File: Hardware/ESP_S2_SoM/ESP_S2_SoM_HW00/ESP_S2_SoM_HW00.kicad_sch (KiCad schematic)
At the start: 0 parts

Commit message: lots of work on routing
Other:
- sheet 100_Connectors ports: added BATTERY_TEMP; removed none
- sheet 200_1S_Charger ports: added BATTERY_TEMP; removed none
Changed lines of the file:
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@@
+    (stroke (width 0) (type default))
+  )
+  (wire (pts (xy 101.6 58.42) (xy 127 58.42))
     (stroke (width 0) (type default))
   )
@@
       (effects (font (size 1.27 1.27)) (justify left))
     )
+    (pin "BATTERY_TEMP" input (at 127 58.42 180)
+      (effects (font (size 1.27 1.27)) (justify left))
+    )
     (instances
       (project "ESP_S2_SoM_HW00"
@@
       (effects (font (size 1.27 1.27)) (justify right))
     )
+    (pin "BATTERY_TEMP" output (at 101.6 58.42 0)
+      (effects (font (size 1.27 1.27)) (justify right))
+    )

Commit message: Working on PSoM ESP32S2
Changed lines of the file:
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@@
     (stroke (width 0) (type default))
+  )
+  (label "3V3" (at 88.9 22.86 90) (fields_autoplaced)
+    (effects (font (size 1.27 1.27)) (justify left bottom))
+  )
+  (label "3V3" (at 88.9 99.06 90) (fields_autoplaced)
+    (effects (font (size 1.27 1.27)) (justify left bottom))
+  )
+  (label "3V3" (at 160.02 99.06 90) (fields_autoplaced)
+    (effects (font (size 1.27 1.27)) (justify left bottom))
+  )
+  (label "VBUS" (at 96.52 22.86 90) (fields_autoplaced)
+    (effects (font (size 1.27 1.27)) (justify left bottom))
+  )
+  (label "VSYS" (at 147.32 22.86 90) (fields_autoplaced)
+    (effects (font (size 1.27 1.27)) (justify left bottom))
+  )
+  (label "VBUS" (at 152.4 22.86 90) (fields_autoplaced)
+    (effects (font (size 1.27 1.27)) (justify left bottom))
+  )
+  (label "VSYS" (at 91.44 22.86 90) (fields_autoplaced)
+    (effects (font (size 1.27 1.27)) (justify left bottom))
+  )
+  (label "VSYS" (at 91.44 99.06 90) (fields_autoplaced)
+    (effects (font (size 1.27 1.27)) (justify left bottom))
+  )
+  (label "VBAT" (at 149.86 22.86 90) (fields_autoplaced)
+    (effects (font (size 1.27 1.27)) (justify left bottom))
+  )
+  (label "VBAT" (at 93.98 22.86 90) (fields_autoplaced)
+    (effects (font (size 1.27 1.27)) (justify left bottom))
   )
   (symbol (lib_id "power:GND") (at 167.64 154.94 0) (unit 1)

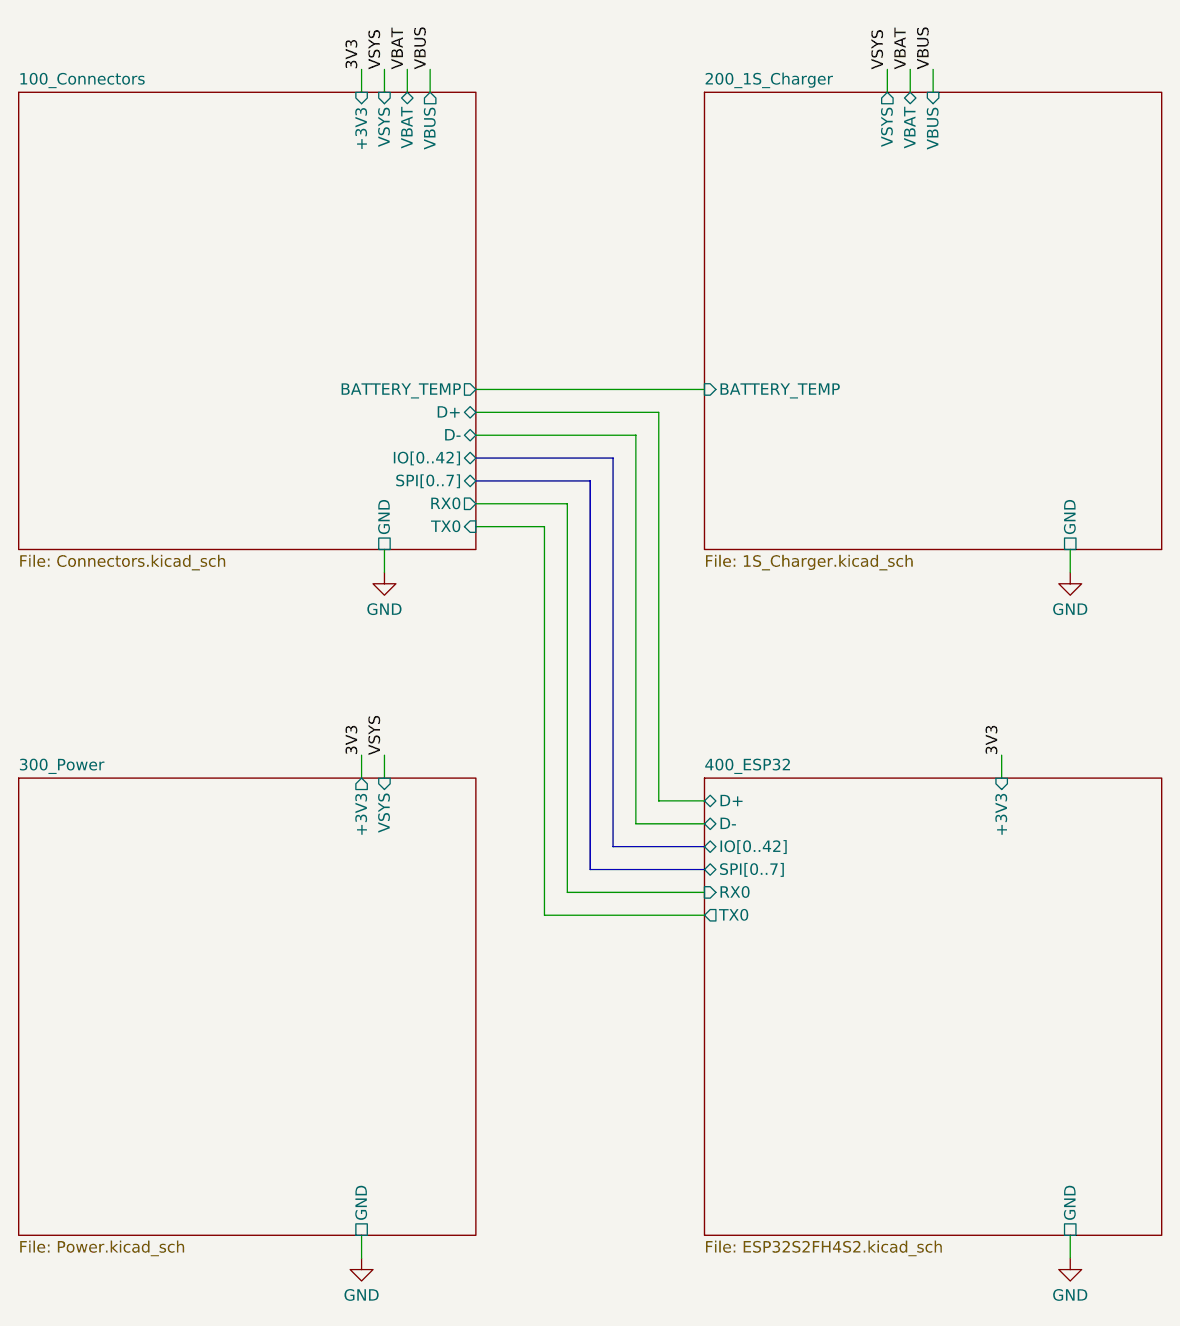
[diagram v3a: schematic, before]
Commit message: quick pinout adjustement
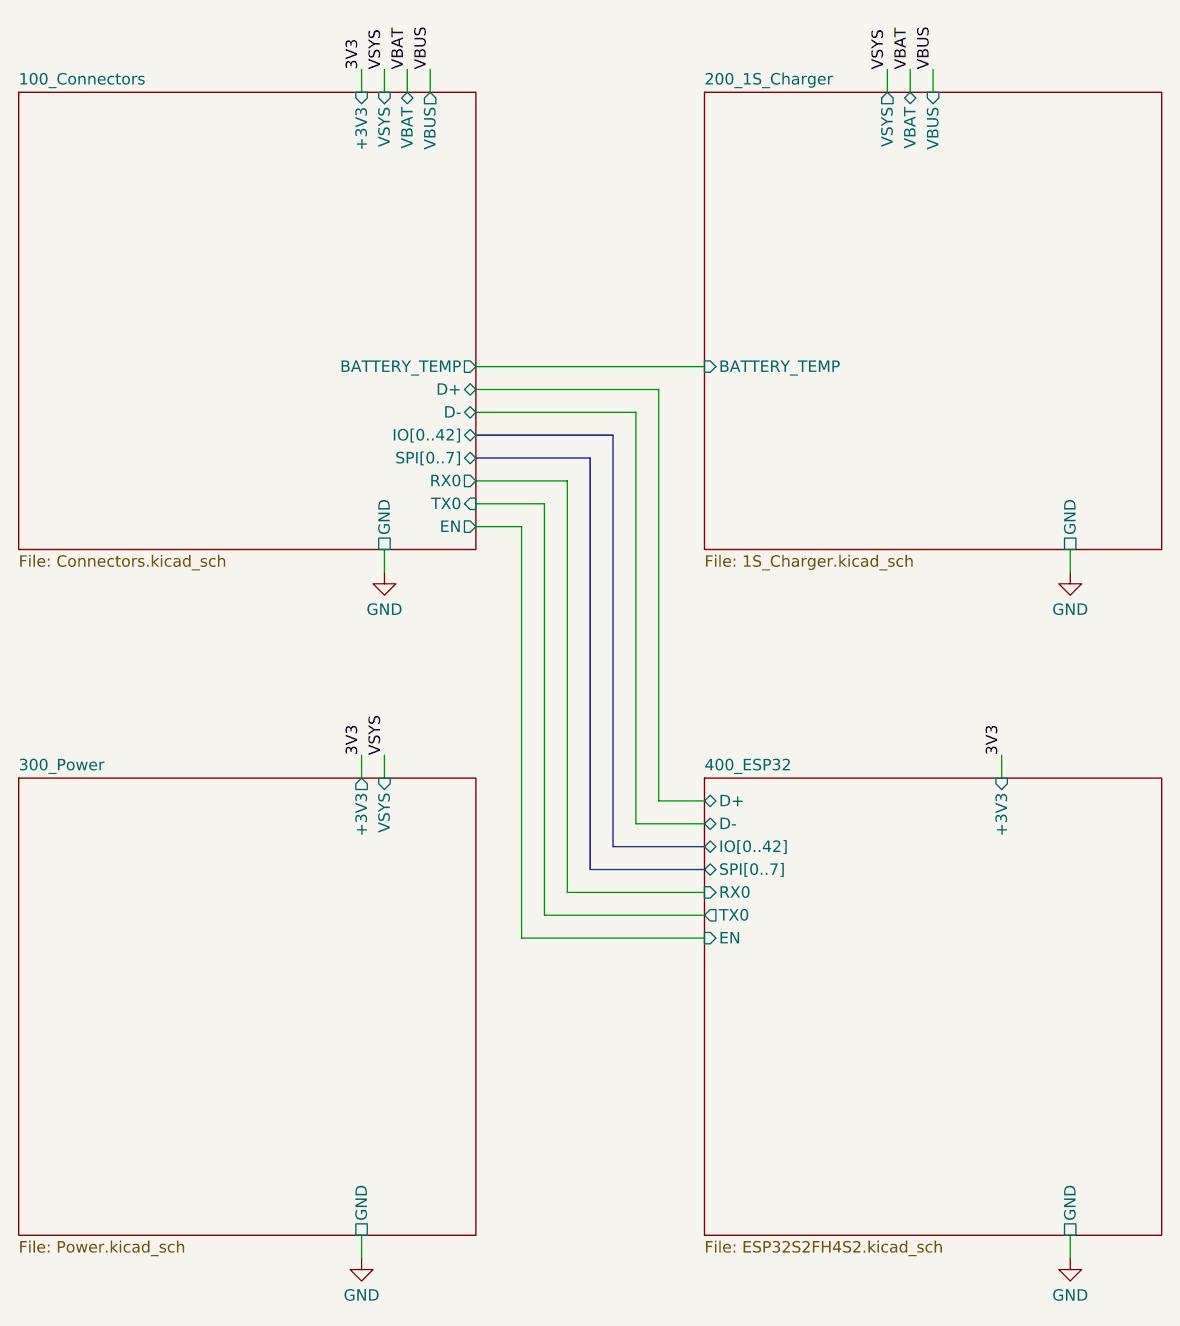
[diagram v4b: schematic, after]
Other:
- sheet 100_Connectors ports: added EN; removed none
- sheet 400_ESP32 ports: added EN; removed none
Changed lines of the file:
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@@
     (company "PumaCorp")
   )
+  (wire (pts (xy 127 114.3) (xy 111.76 114.3))
+    (stroke (width 0) (type default))
+  )
+  (wire (pts (xy 147.32 22.86) (xy 147.32 25.4))
+    (stroke (width 0) (type default))
+  )
+  (bus (pts (xy 114.3 111.76) (xy 127 111.76))
+    (stroke (width 0) (type default))
+  )
+  (wire (pts (xy 167.64 152.4) (xy 167.64 154.94))
+    (stroke (width 0) (type default))
+  )
+  (wire (pts (xy 93.98 22.86) (xy 93.98 25.4))
+    (stroke (width 0) (type default))
+  )
+  (wire (pts (xy 109.22 71.12) (xy 109.22 116.84))
+    (stroke (width 0) (type default))
+  )
+  (wire (pts (xy 96.52 22.86) (xy 96.52 25.4))
+    (stroke (width 0) (type default))
+  )
+  (wire (pts (xy 101.6 73.66) (xy 106.68 73.66))
+    (stroke (width 0) (type default))
+  )
+  (wire (pts (xy 91.44 76.2) (xy 91.44 78.74))
+    (stroke (width 0) (type default))
+  )
+  (wire (pts (xy 121.92 58.42) (xy 101.6 58.42))
+    (stroke (width 0) (type default))
+  )
+  (wire (pts (xy 106.68 73.66) (xy 106.68 119.38))
+    (stroke (width 0) (type default))
+  )
+  (wire (pts (xy 121.92 58.42) (xy 121.92 104.14))
+    (stroke (width 0) (type default))
+  )
+  (wire (pts (xy 111.76 114.3) (xy 111.76 68.58))
+    (stroke (width 0) (type default))
+  )
+  (wire (pts (xy 88.9 152.4) (xy 88.9 154.94))
+    (stroke (width 0) (type default))
+  )
+  (bus (pts (xy 116.84 109.22) (xy 116.84 63.5))
+    (stroke (width 0) (type default))
+  )
+  (bus (pts (xy 127 109.22) (xy 116.84 109.22))
+    (stroke (width 0) (type default))
+  )
+  (wire (pts (xy 106.68 119.38) (xy 127 119.38))
+    (stroke (width 0) (type default))
+  )
+  (wire (pts (xy 111.76 68.58) (xy 101.6 68.58))
+    (stroke (width 0) (type default))
+  )
   (wire (pts (xy 119.38 106.68) (xy 127 106.68))
     (stroke (width 0) (type default))
   )
-  (wire (pts (xy 147.32 22.86) (xy 147.32 25.4))
-    (stroke (width 0) (type default))
-  )
-  (wire (pts (xy 167.64 152.4) (xy 167.64 154.94))
-    (stroke (width 0) (type default))
-  )
-  (wire (pts (xy 93.98 22.86) (xy 93.98 25.4))
-    (stroke (width 0) (type default))
-  )
-  (wire (pts (xy 101.6 73.66) (xy 109.22 73.66))
-    (stroke (width 0) (type default))
-  )
-  (wire (pts (xy 96.52 22.86) (xy 96.52 25.4))
-    (stroke (width 0) (type default))
-  )
-  (wire (pts (xy 111.76 71.12) (xy 101.6 71.12))
-    (stroke (width 0) (type default))
-  )
-  (wire (pts (xy 119.38 63.5) (xy 119.38 106.68))
-    (stroke (width 0) (type default))
-  )
-  (wire (pts (xy 91.44 76.2) (xy 91.44 78.74))
-    (stroke (width 0) (type default))
-  )
-  (wire (pts (xy 121.92 104.14) (xy 121.92 60.96))
-    (stroke (width 0) (type default))
-  )
-  (bus (pts (xy 114.3 68.58) (xy 114.3 111.76))
-    (stroke (width 0) (type default))
-  )
-  (wire (pts (xy 121.92 60.96) (xy 101.6 60.96))
-    (stroke (width 0) (type default))
-  )
-  (wire (pts (xy 88.9 152.4) (xy 88.9 154.94))
+  (bus (pts (xy 114.3 66.04) (xy 114.3 111.76))
+    (stroke (width 0) (type default))
+  )
+  (wire (pts (xy 91.44 22.86) (xy 91.44 25.4))
+    (stroke (width 0) (type default))
+  )
+  (wire (pts (xy 167.64 76.2) (xy 167.64 78.74))
     (stroke (width 0) (type default))
   )
@@
     (stroke (width 0) (type default))
   )
-  (bus (pts (xy 101.6 68.58) (xy 114.3 68.58))
-    (stroke (width 0) (type default))
-  )
-  (wire (pts (xy 91.44 22.86) (xy 91.44 25.4))
-    (stroke (width 0) (type default))
-  )
-  (wire (pts (xy 111.76 114.3) (xy 111.76 71.12))
-    (stroke (width 0) (type default))
-  )
-  (wire (pts (xy 167.64 76.2) (xy 167.64 78.74))
-    (stroke (width 0) (type default))
-  )
-  (bus (pts (xy 116.84 66.04) (xy 101.6 66.04))
-    (stroke (width 0) (type default))
-  )
-  (wire (pts (xy 127 114.3) (xy 111.76 114.3))
-    (stroke (width 0) (type default))
-  )
-  (wire (pts (xy 101.6 63.5) (xy 119.38 63.5))
+  (wire (pts (xy 101.6 71.12) (xy 109.22 71.12))
     (stroke (width 0) (type default))
   )
@@
     (stroke (width 0) (type default))
   )
-  (wire (pts (xy 109.22 73.66) (xy 109.22 116.84))
-    (stroke (width 0) (type default))
-  )
   (wire (pts (xy 152.4 22.86) (xy 152.4 25.4))
     (stroke (width 0) (type default))
   )
-  (bus (pts (xy 116.84 109.22) (xy 116.84 66.04))
+  (wire (pts (xy 119.38 60.96) (xy 119.38 106.68))
+    (stroke (width 0) (type default))
+  )
+  (bus (pts (xy 101.6 66.04) (xy 114.3 66.04))
+    (stroke (width 0) (type default))
+  )
+  (wire (pts (xy 101.6 60.96) (xy 119.38 60.96))
+    (stroke (width 0) (type default))
+  )
+  (bus (pts (xy 116.84 63.5) (xy 101.6 63.5))
     (stroke (width 0) (type default))
   )
@@
     (stroke (width 0) (type default))
   )
-  (wire (pts (xy 101.6 58.42) (xy 127 58.42))
-    (stroke (width 0) (type default))
-  )
-  (bus (pts (xy 127 109.22) (xy 116.84 109.22))
+  (wire (pts (xy 101.6 55.88) (xy 127 55.88))
     (stroke (width 0) (type default))
   )
@@
   )
   (wire (pts (xy 88.9 99.06) (xy 88.9 101.6))
-    (stroke (width 0) (type default))
-  )
-  (bus (pts (xy 114.3 111.76) (xy 127 111.76))
     (stroke (width 0) (type default))
   )
@@
       (effects (font (size 1.27 1.27)) (justify left))
     )
-    (pin "BATTERY_TEMP" input (at 127 58.42 180)
+    (pin "BATTERY_TEMP" input (at 127 55.88 180)
       (effects (font (size 1.27 1.27)) (justify left))
     )
@@
       (effects (font (size 1.27 1.27)) (justify left top))
     )
-    (pin "D-" bidirectional (at 101.6 63.5 0)
+    (pin "D-" bidirectional (at 101.6 60.96 0)
       (effects (font (size 1.27 1.27)) (justify right))
     )
@@
       (effects (font (size 1.27 1.27)) (justify right))
     )
-    (pin "D+" bidirectional (at 101.6 60.96 0)
+    (pin "D+" bidirectional (at 101.6 58.42 0)
       (effects (font (size 1.27 1.27)) (justify right))
     )
@@
       (effects (font (size 1.27 1.27)) (justify left))
     )
-    (pin "IO[0..42]" bidirectional (at 101.6 66.04 0)
+    (pin "IO[0..42]" bidirectional (at 101.6 63.5 0)
       (effects (font (size 1.27 1.27)) (justify right))
     )
@@
       (effects (font (size 1.27 1.27)) (justify right))
     )
-    (pin "TX0" input (at 101.6 73.66 0)
-      (effects (font (size 1.27 1.27)) (justify right))
-    )
-    (pin "RX0" output (at 101.6 71.12 0)
-      (effects (font (size 1.27 1.27)) (justify right))
-    )
-    (pin "SPI[0..7]" bidirectional (at 101.6 68.58 0)
-      (effects (font (size 1.27 1.27)) (justify right))
-    )
-    (pin "BATTERY_TEMP" output (at 101.6 58.42 0)
+    (pin "TX0" input (at 101.6 71.12 0)
+      (effects (font (size 1.27 1.27)) (justify right))
+    )
+    (pin "RX0" output (at 101.6 68.58 0)
+      (effects (font (size 1.27 1.27)) (justify right))
+    )
+    (pin "SPI[0..7]" bidirectional (at 101.6 66.04 0)
+      (effects (font (size 1.27 1.27)) (justify right))
+    )
+    (pin "BATTERY_TEMP" output (at 101.6 55.88 0)
+      (effects (font (size 1.27 1.27)) (justify right))
+    )
+    (pin "EN" output (at 101.6 73.66 0)
       (effects (font (size 1.27 1.27)) (justify right))
     )
@@
       (effects (font (size 1.27 1.27)) (justify left))
     )
+    (pin "EN" input (at 127 119.38 180)
+      (effects (font (size 1.27 1.27)) (justify left))
+    )

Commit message: Small cartouche mistake
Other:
- title: PSoM - ESP S3 -> PSoM - ESP S2
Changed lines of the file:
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@@
   (paper "A4")
   (title_block
-    (title "PSoM - ESP S3")
+    (title "PSoM - ESP S2")
     (date "2023-04-17")
     (rev "HW00")
